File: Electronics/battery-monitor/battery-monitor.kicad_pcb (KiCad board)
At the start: 2 copper layers, 71.1 x 38.1 mm, 20 parts, among them IC1 ATMEGA328P-P, J1 Screw_Terminal_1x02, J2 Screw_Terminal_1x02, J3 Screw_Terminal_1x02, J4 Screw_Terminal_1x02, J5 Screw_Terminal_1x02, U1 ACS714LLCTR-30A-T, U2 LM7805CT, Y1 Crystal

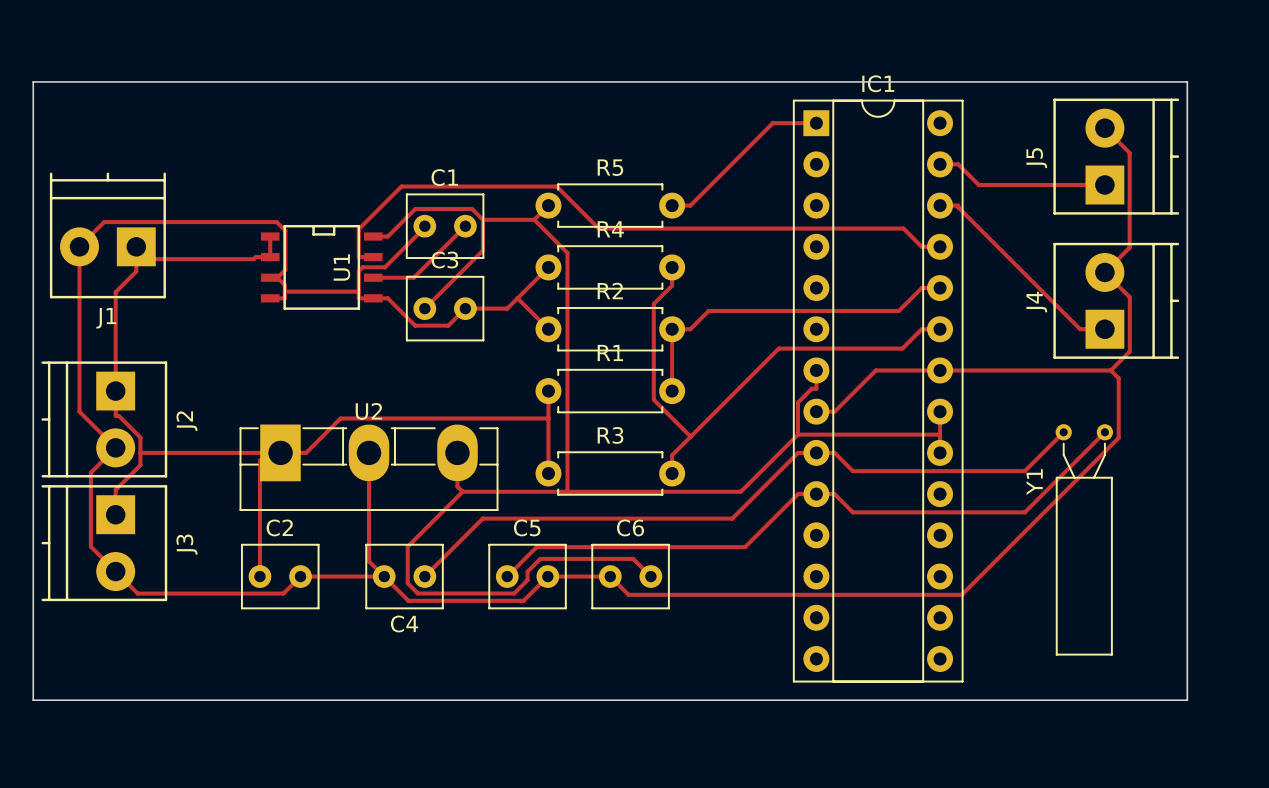
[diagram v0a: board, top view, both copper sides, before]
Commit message: cleaned up board files and finally made a successful cut on the battery monitor
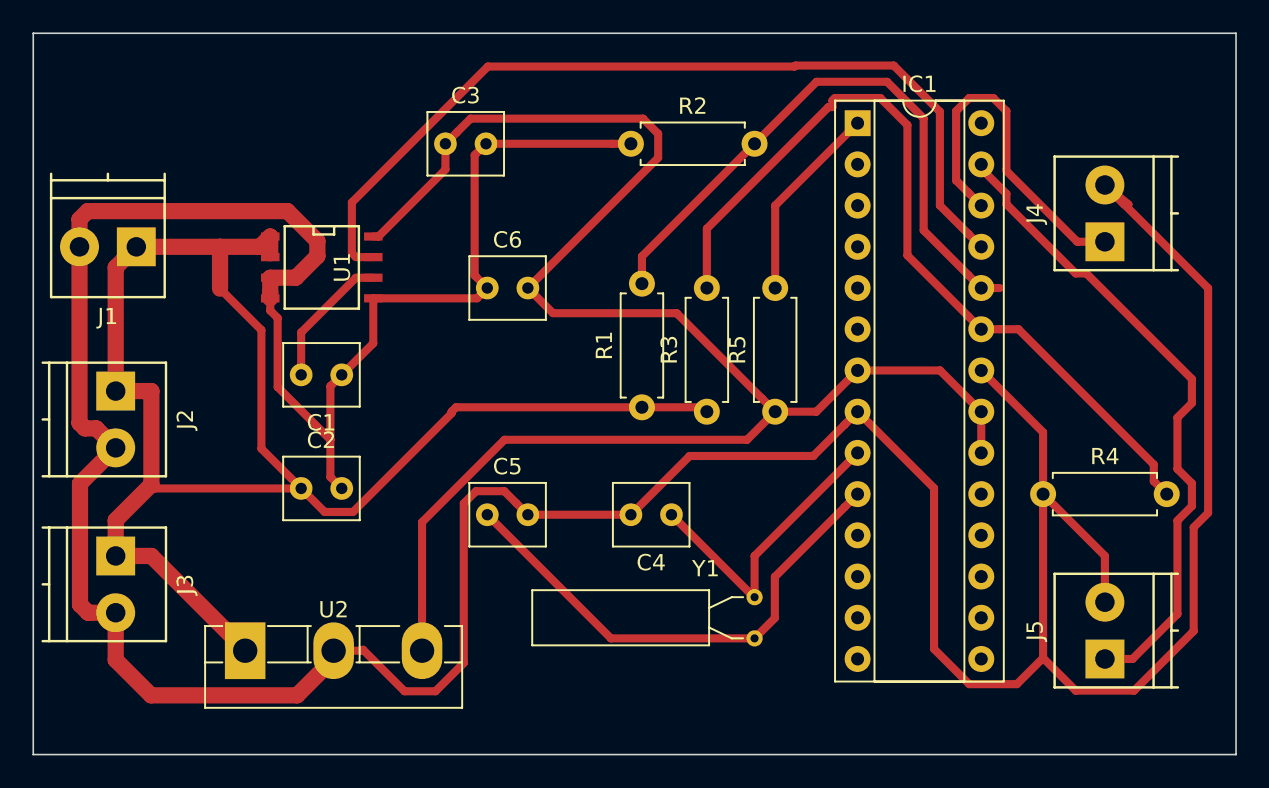
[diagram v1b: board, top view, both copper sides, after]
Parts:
- moved R4 33.5 mm to (172.7, 133.3)
- moved J5 29.2 mm to (176.5, 143.5)
- moved Y1 21.6 mm to (154.9, 139.7), turned to 270 degrees
- moved C6 19.3 mm to (138.5, 120.7)
- moved R5 18.9 mm to (156.2, 128.3), turned to 90 degrees
- moved C4 15.7 mm to (149.8, 134.6)
- moved R2 12.5 mm to (147.3, 111.8)
- moved U2 12.4 mm to (123.5, 143.0)
- moved C1 10.5 mm to (129.5, 126.0), turned to 180 degrees
- moved R3 10.5 mm to (152.0, 128.3), turned to 90 degrees
- moved C3 10.2 mm to (135.9, 111.8)
- moved C2 5.99 mm to (127.0, 133.0)
- moved R1 5.85 mm to (148.0, 128.0), turned to 90 degrees
- moved J4 5.39 mm to (176.5, 117.8)
- moved C5 4.00 mm to (138.5, 134.6)
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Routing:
- net Net-(C1-Pad1): track 187.1 -> 263.5 mm
- net Net-(C2-Pad1): track 66.9 -> 97.4 mm
- net Net-(IC1-Pad27): track 10.7 -> 40.2 mm
- net Net-(C4-Pad1): track 44.0 -> 18.7 mm
- net Net-(IC1-Pad23): track 32.7 -> 51.0 mm
- net Net-(IC1-Pad24): track 21.4 -> 37.5 mm
- net Net-(IC1-Pad25): track 41.1 -> 54.8 mm
- net Net-(C5-Pad1): track 41.4 -> 31.1 mm
- net Net-(IC1-Pad26): track 13.4 -> 21.8 mm
- net Net-(C3-Pad1): track 101.2 -> 103.0 mm
- net Net-(C1-Pad2): track 6.99 -> 8.45 mm
- net Net-(IC1-Pad1): track 11.0 -> 12.3 mm
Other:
- board size 71.1 x 38.1 mm -> 74.1 x 44.5 mm
- net class Default: clearance 0.2 -> 0.5; trace_width 0.25 -> 0.5
- net class power added: clearance 0.5, trace_width 1, via_dia 0.6, via_drill 0.4
- rule trace_clearance: 0.2 -> 0.5
- rule trace_min: 0.2 -> 0.5
